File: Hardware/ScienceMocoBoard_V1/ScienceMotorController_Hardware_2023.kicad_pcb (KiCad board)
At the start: 2 copper layers, 124.6 x 81.3 mm, 134 parts, among them Q1 SI4156DY, Q10 SI4156DY, Q11 SI4156DY, Q12 SI4156DY, Q13 SI4156DY, Q14 SI4156DY, Q15 SI4156DY, Q16 SI4156DY, Q2 SI4156DY, Q3 SI4156DY, Q4 SI4156DY, Q5 SI4156DY, Q6 SI4156DY, Q7 SI4156DY, Q8 SI4156DY, Q9 SI4156DY, U1 IRS2005S, U10 IRS2005S, U11 TM4C129E_Launchpad, U2 IRS2005S, U3 3V3 OKI, U4 TSR_1-2450, U5 IRS2005S, U6 IRS2005S, U7 IRS2005S, U8 IRS2005S, U9 IRS2005S

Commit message: Started Layout Design
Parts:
- added G***: LOGO, MRDT_Silkscreens:0_MRDT_Logo_7.5mm, F.Cu at (-109.7, 145.0)
- added G***: LOGO, LOGO, F.Cu at (-106.2, 124.0)
- added G***: LOGO, LOGO, F.Cu at (-93.6, 73.5)
- moved D31 264.2 mm to (120.0, -125.0), turned to 180 degrees
- moved D30 244.6 mm to (120.0, -115.0), turned to 180 degrees
- moved LimSwitch6 243.3 mm to (105.0, -125.0)
- moved R38 233.6 mm to (115.0, -115.0)
- moved R39 231.2 mm to (115.0, -125.0)
- moved R37 203.8 mm to (115.0, -105.0)
- moved D29 201.0 mm to (120.0, -105.0), turned to 180 degrees
- moved LimSwitch5 187.1 mm to (105.0, -115.0)
- moved Re 186.1 mm to (115.0, -95.0)
- moved LimSwitch4 183.4 mm to (105.0, -105.0)
- moved LimSwitch2 181.3 mm to (105.0, -95.0)
- moved D27 179.3 mm to (120.0, -95.0), turned to 180 degrees
- moved R34 177.5 mm to (115.0, -85.0), turned to 180 degrees
- moved R36 171.0 mm to (115.0, -75.0)
- moved LimSwitch1 167.2 mm to (105.0, -85.0)
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- renumbered R35 to Re
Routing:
- removed copper zone on B.Cu, net GND
- removed copper zone on F.Cu, net GND
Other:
- board size 124.6 x 81.3 mm -> 187 x 127 mm

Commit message: Organized Layout
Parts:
- moved R16 280.5 mm to (54.6, 255.3), turned to 90 degrees
- moved D12 264.1 mm to (53.2, 283.1)
- moved C3 263.2 mm to (398.6, 120.8)
- moved C10 263.2 mm to (407.0, 116.9)
- moved Conn5 263.2 mm to (308.9, 134.3)
- moved Conn6 263.2 mm to (320.2, 116.7)
- moved D15 263.2 mm to (381.7, 136.3)
- moved D16 263.2 mm to (355.3, 139.3)
- moved D23 263.2 mm to (342.2, 139.4)
- moved D7 263.2 mm to (313.4, 126.5)
- moved Q12 263.2 mm to (375.2, 130.3)
- moved Q13 263.2 mm to (366.8, 131.8)
- moved Q14 263.2 mm to (366.8, 138.3)
- moved Q15 263.2 mm to (383.7, 122.8)
- moved R21 263.2 mm to (386.0, 136.2)
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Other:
- board text added: "Encoders"
- board text added: "Limit Swithches"
- board text added: "Power"
- board text added: "Servos"
- board text added: "X-Axis"

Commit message: Layout for Encoders, Servos, and Limit Switches
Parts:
- removed the G*** at (-109.7, 145.0)
- Conn1, Conn2, Conn3, Conn4, Conn5, Conn6, Conn7: footprint MRDT_Connectors:Square_Anderson_2_V_Side_By_Side -> MRDT_Connectors:Square_Anderson_2_H_Side_By_Side
- moved R39 260.8 mm to (91.8, 134.7), turned to 90 degrees
- moved D31 260.8 mm to (96.9, 134.7), turned to -90 degrees
- moved LimSwitch6 253.9 mm to (93.1, 128.7)
- moved R38 252.3 mm to (79.4, 134.7), turned to 90 degrees
- moved D30 252.1 mm to (85.5, 134.7), turned to -90 degrees
- moved D29 245.5 mm to (73.3, 136.0), turned to -90 degrees
- moved R37 245.1 mm to (68.3, 135.6), turned to 90 degrees
- moved LimSwitch5 245.1 mm to (81.3, 128.9)
- moved LimSwitch4 236.8 mm to (68.8, 129.0)
- moved D13 221.2 mm to (96.8, 87.0), turned to 90 degrees
- moved R19 217.8 mm to (101.9, 87.0), turned to -90 degrees
- moved D12 217.1 mm to (146.5, 87.0), turned to 90 degrees
- moved D27 215.2 mm to (96.6, 118.9), turned to -90 degrees
- moved R35 214.7 mm to (92.4, 118.5), turned to 90 degrees
- moved R18 214.6 mm to (151.5, 87.0), turned to -90 degrees
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- renumbered Re to R35
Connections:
- R36 pad 2: unconnected-(R36-Pad2) -> Limit_Switch_1
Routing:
- net GND: track 0.00 -> 86.5 mm
- net +5V: track 0.00 -> 74.6 mm
- net Servo_3: track 0.00 -> 46.0 mm, vias 0 -> 1
- net Servo_6: track 0.00 -> 37.5 mm
- net Limit_Switch_4: track 0.00 -> 37.2 mm
- net Limit_Switch_6: track 0.00 -> 35.1 mm
- net Limit_Switch_5: track 0.00 -> 33.2 mm
- net Servo_5: track 0.00 -> 27.1 mm
- net Limit_Switch_3: track 0.00 -> 27.0 mm
- net Encoder_PWM_4: track 0.00 -> 26.8 mm
- net Servo_2: track 0.00 -> 26.4 mm
- net Servo_1: track 0.00 -> 23.8 mm
- net +3V3: track 0.00 -> 23.1 mm
- net Limit_Switch_2: track 0.00 -> 19.2 mm
- net Limit_Switch_1: track 0.00 -> 18.0 mm
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- added copper zone on B.Cu, net GND
- added copper zone on F.Cu, net GND

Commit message: Power on Layout. Organized H-Bridge Components
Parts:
- moved U2 387.3 mm to (45.0, -37.1)
- moved C3 381.6 mm to (51.3, -37.3)
- moved Q3 366.3 mm to (65.3, -42.4)
- moved Q4 358.3 mm to (66.0, -32.0)
- moved D2 336.5 mm to (32.3, -40.1)
- moved D7 336.3 mm to (49.3, -42.7)
- moved D15 321.0 mm to (118.4, -47.2)
- moved D5 319.9 mm to (37.8, -40.1)
- moved R9 315.3 mm to (56.9, -34.3)
- moved R2 312.1 mm to (32.0, -34.5)
- moved R5 304.6 mm to (37.3, -33.8)
- moved R21 303.9 mm to (164.1, -71.4)
- moved U6 298.7 mm to (127.0, -36.3)
- moved R26 294.2 mm to (184.9, -79.2)
- moved C10 293.7 mm to (184.5, -74.8), turned to -90 degrees
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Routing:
- net GND: track 86.5 -> 29.6 mm
- net +3V3: track 23.1 -> 41.3 mm
- net +5V: track 74.6 -> 84.7 mm
- net +12V: track 0.00 -> 8.88 mm
- net Net-(D9-Pad2): track 0.00 -> 5.10 mm
- net Net-(D8-Pad2): track 0.00 -> 4.27 mm
- net Net-(D3-Pad2): track 0.00 -> 3.55 mm
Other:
- board size 187 x 127 mm -> 179.9 x 127 mm
- board text added: "Science-Z"
- board text added: "Scoop-Z"

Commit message: Attempted an H-Bridge
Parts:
- moved D1 134.5 mm to (65.8, 49.9), turned to 180 degrees
- moved D6 131.0 mm to (61.3, 44.6), turned to -90 degrees
- moved C5 129.7 mm to (99.1, 48.5), turned to 180 degrees
- moved R1 129.6 mm to (61.6, 49.9), turned to 180 degrees
- moved R4 127.4 mm to (82.7, 49.7)
- moved D4 127.4 mm to (77.2, 49.7)
- moved U1 127.1 mm to (71.2, 44.7), turned to 90 degrees
- moved R7 125.8 mm to (78.4, 42.2)
- moved Q1 122.0 mm to (85.6, 37.4), turned to 180 degrees
- moved Conn4 121.3 mm to (103.3, 43.9), turned to -90 degrees
- moved Q2 119.0 mm to (85.6, 43.5)
- moved C2 116.9 mm to (70.6, 38.4)
- moved R6 112.9 mm to (78.5, 38.2), turned to 0 degrees
- moved Q5 112.4 mm to (113.3, 31.0)
- moved D14 112.1 mm to (128.8, 27.9), turned to 180 degrees
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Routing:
- net +12V: track 8.88 -> 22.3 mm
- net Net-(C2-Pad1): track 0.00 -> 12.7 mm
- net RVS_PWM_1: track 0.00 -> 12.0 mm
- net FWD_PWM_1: track 0.00 -> 11.6 mm
- net Net-(R12-Pad1): track 0.00 -> 11.3 mm
- net /M-: track 0.00 -> 11.0 mm
- net /M+: track 0.00 -> 10.2 mm
- net Net-(R6-Pad1): track 0.00 -> 9.82 mm, vias 0 -> 2
- net Net-(Q1-Pad4): track 0.00 -> 9.76 mm
- net Net-(R13-Pad1): track 0.00 -> 9.49 mm
- net Net-(C7-Pad1): track 0.00 -> 8.66 mm
- net Net-(Q2-Pad4): track 0.00 -> 6.05 mm
- net Net-(Q5-Pad4): track 0.00 -> 4.61 mm
- net Net-(R7-Pad1): track 0.00 -> 4.38 mm
- net Net-(Q6-Pad4): track 0.00 -> 4.36 mm
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
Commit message: Reworked Layout to be better
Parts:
- moved D24 158.0 mm to (197.6, 122.2), turned to 90 degrees
- moved R32 157.9 mm to (197.6, 112.5), turned to -90 degrees
- moved D25 155.9 mm to (200.2, 127.5), turned to 90 degrees
- moved R33 155.2 mm to (200.2, 117.9), turned to 90 degrees
- moved R1 102.4 mm to (162.3, 68.6), turned to -90 degrees
- moved R37 99.0 mm to (153.2, 133.5)
- moved R38 98.0 mm to (163.3, 133.5)
- moved D6 96.6 mm to (156.5, 61.5)
- moved D1 96.4 mm to (160.4, 68.6), turned to 90 degrees
- moved LimSwitch4 95.9 mm to (150.6, 127.4)
- moved R39 95.8 mm to (173.5, 133.5)
- moved R7 94.8 mm to (173.2, 40.1), turned to 90 degrees
- moved LimSwitch5 93.7 mm to (160.8, 127.4)
- moved LimSwitch6 92.0 mm to (170.9, 127.4)
- moved D4 91.6 mm to (166.9, 68.6), turned to 90 degrees
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- renumbered D28 to D26, D26 to D27, D27 to D28, LimSwitch3 to LimSwitch1, LimSwitch1 to LimSwitch2, LimSwitch2 to LimSwitch3, R36 to R34, R34 to R35, R35 to R36
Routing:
- net +5V: track 84.7 -> 0.36 mm
- net Servo_3: track 46.0 -> 0.00 mm, vias 1 -> 0
- net +3V3: track 41.3 -> 0.00 mm
- net Servo_6: track 37.5 -> 0.00 mm
- net Limit_Switch_4: track 37.2 -> 0.00 mm
- net Limit_Switch_6: track 35.1 -> 0.00 mm
- net Limit_Switch_5: track 33.2 -> 0.00 mm
- net GND: track 29.6 -> 0.54 mm
- net Servo_5: track 27.1 -> 0.00 mm
- net Limit_Switch_3: track 27.0 -> 0.00 mm
- net Encoder_PWM_4: track 26.8 -> 0.00 mm
- net Servo_2: track 26.4 -> 0.00 mm
- net Servo_1: track 23.8 -> 0.00 mm
- net +12V: track 22.3 -> 0.00 mm
- net Limit_Switch_2: track 19.2 -> 0.00 mm
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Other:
- board size 179.9 x 127 mm -> 231.4 x 127 mm
- board text added: "Limit Switches"
- board text removed: "Limit Swithches"

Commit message: Added H-Bridges. Started Traces
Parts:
- Conn4, Conn5, Conn6, Conn7: moved to B.Cu
- moved D23 169.5 mm to (164.2, 60.4), turned to -90 degrees
- moved D5 162.2 mm to (159.0, 67.8)
- moved D2 160.9 mm to (151.6, 67.8)
- moved R5 159.6 mm to (159.0, 69.4), turned to 180 degrees
- moved R2 158.5 mm to (151.6, 69.4), turned to 180 degrees
- moved U10 158.2 mm to (167.9, 62.0), turned to 90 degrees
- moved R30 154.7 mm to (169.0, 55.6)
- moved C14 150.7 mm to (166.1, 56.4), turned to 90 degrees
- moved U2 149.9 mm to (157.5, 61.9), turned to 90 degrees
- moved Q15 148.8 mm to (167.9, 50.9), turned to 90 degrees
- moved D7 147.8 mm to (153.8, 61.7), turned to -90 degrees
- moved D19 145.3 mm to (177.5, 68.0)
- moved D17 145.1 mm to (169.5, 67.8)
- moved D21 141.9 mm to (172.2, 60.5), turned to -90 degrees
- moved R23 141.8 mm to (177.5, 69.8), turned to 180 degrees
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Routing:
- net Limit_Switch_6: track 0.00 -> 56.0 mm
- net Limit_Switch_5: track 0.00 -> 51.4 mm
- net Limit_Switch_4: track 0.00 -> 42.9 mm
- net Limit_Switch_3: track 0.00 -> 34.4 mm
- net Limit_Switch_2: track 0.00 -> 28.4 mm
- net Limit_Switch_1: track 0.00 -> 25.3 mm
- net Net-(D31-Pad2): track 0.00 -> 4.33 mm
- net Net-(D30-Pad2): track 0.00 -> 4.33 mm
- net Net-(D28-Pad2): track 0.00 -> 4.33 mm
- net Net-(D26-Pad2): track 0.00 -> 4.33 mm
- net Net-(D29-Pad2): track 0.00 -> 4.33 mm
- net Net-(D27-Pad2): track 0.00 -> 4.33 mm
- net Net-(D24-Pad2): track 0.00 -> 2.64 mm
- net Net-(D25-Pad2): track 0.00 -> 2.63 mm
- net Net-(R32-Pad1): track 0.00 -> 2.48 mm
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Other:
- board text added: "Spare"

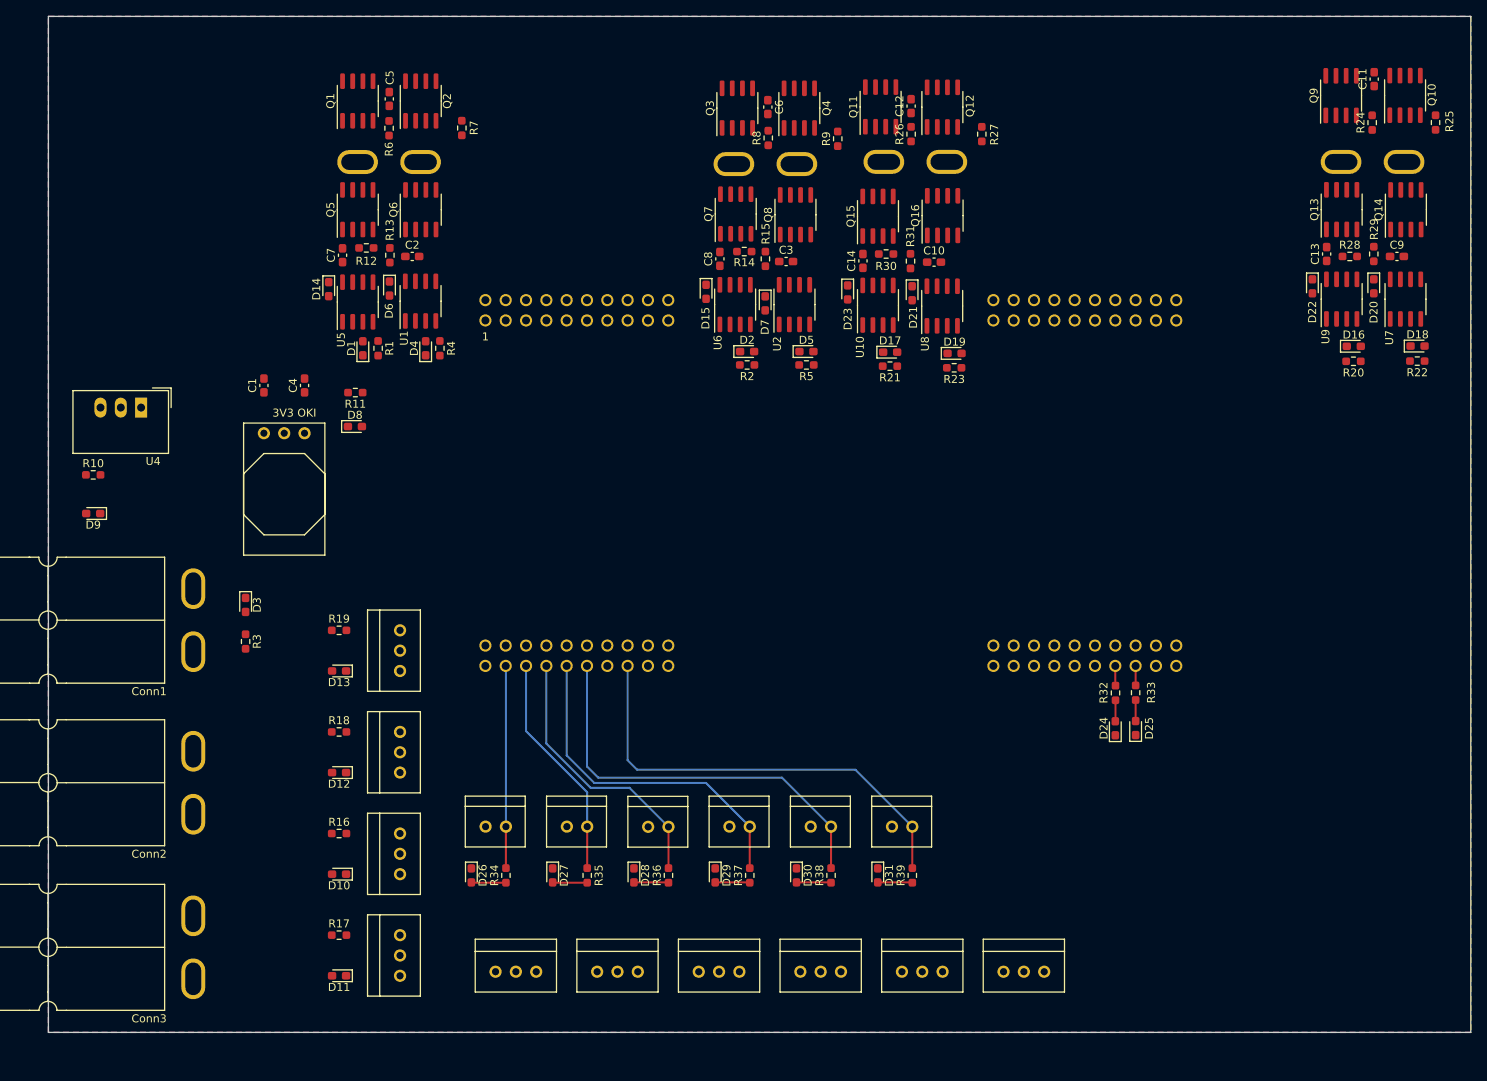
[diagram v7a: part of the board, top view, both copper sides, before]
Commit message: Made traces for servos and encoders
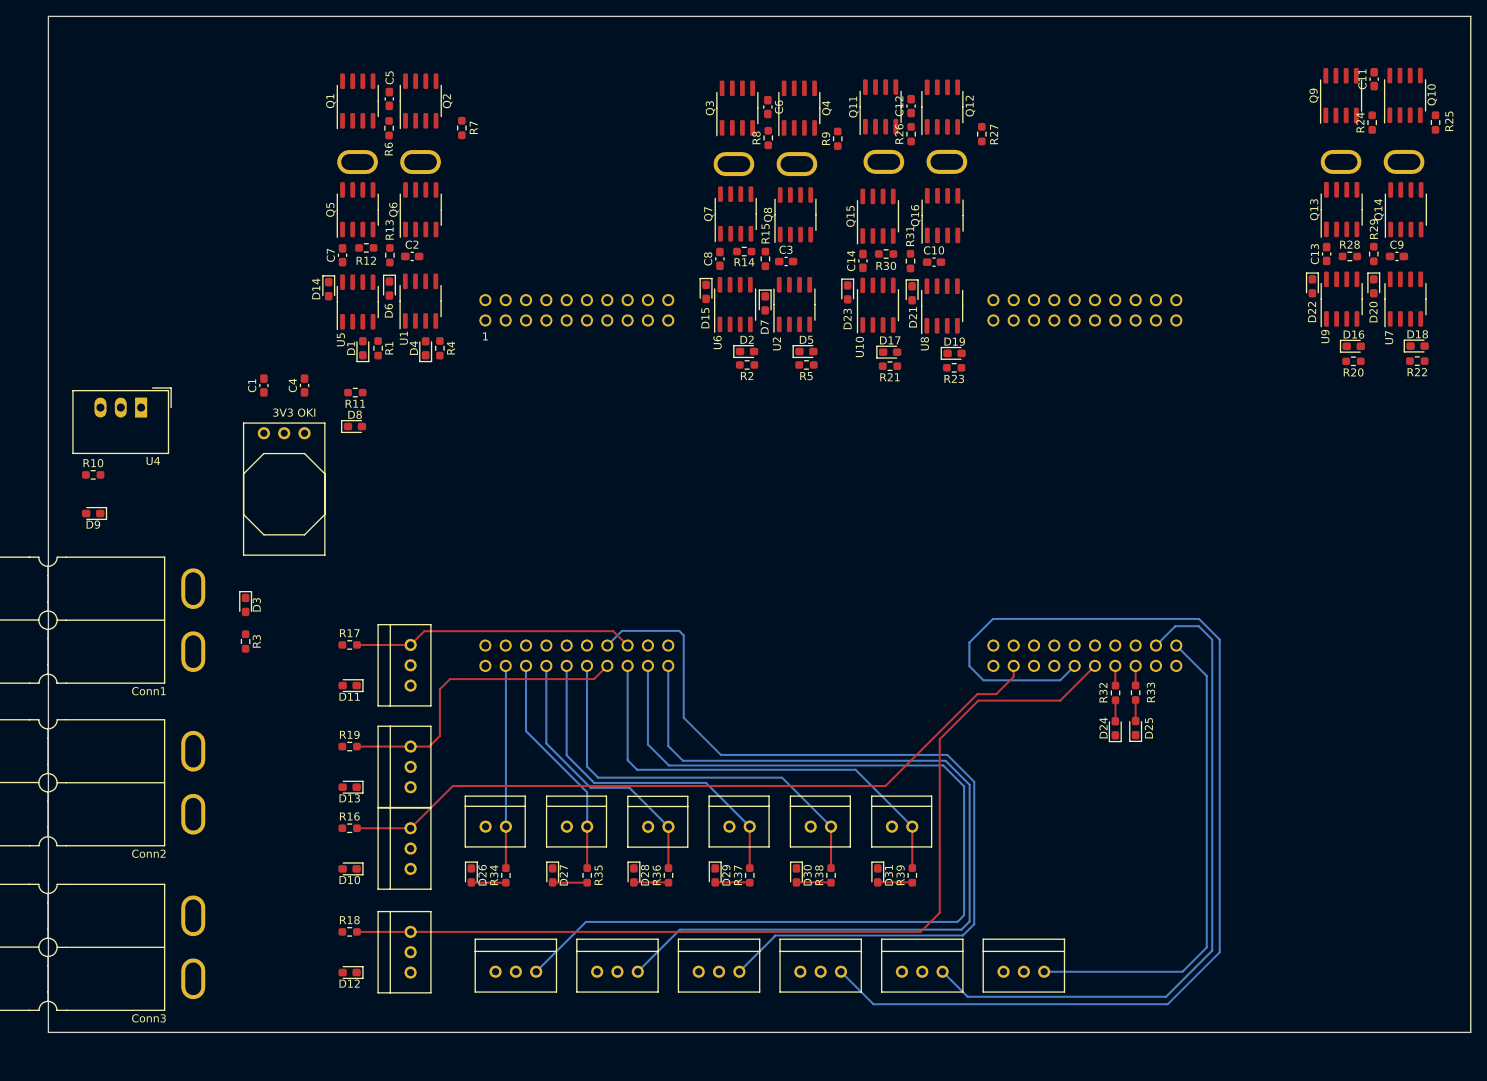
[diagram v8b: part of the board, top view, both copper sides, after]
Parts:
- moved R17 36.3 mm to (101.9, 104.4)
- moved AbsEncode1 36.3 mm to (109.5, 109.5)
- moved D11 36.3 mm to (101.9, 109.5)
- moved AbsEncode2 25.0 mm to (109.5, 145.4)
- moved D12 25.0 mm to (101.9, 145.4)
- moved R18 25.0 mm to (101.9, 140.3)
- moved AbsEncode3 14.6 mm to (109.5, 122.2)
- moved D13 14.6 mm to (101.9, 122.2)
- moved R19 14.6 mm to (101.9, 117.1)
- moved AbsEncode4 1.48 mm to (109.5, 132.4)
- moved D10 1.48 mm to (101.9, 132.4)
- moved R16 1.48 mm to (101.9, 127.4)
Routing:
- net Servo_4: track 0.00 -> 142.0 mm
- net Servo_1: track 0.00 -> 124.0 mm
- net Encoder_PWM_3: track 0.00 -> 118.7 mm
- net Servo_2: track 0.00 -> 110.9 mm
- net Servo_3: track 0.00 -> 110.1 mm
- net Encoder_PWM_2: track 0.00 -> 91.3 mm
- net Servo_5: track 0.00 -> 85.0 mm
- net Servo_6: track 0.00 -> 60.9 mm
- net Encoder_PWM_4: track 0.00 -> 38.9 mm
- net Encoder_PWM_1: track 0.00 -> 35.3 mm
- removed copper zone on B.Cu, net GND
- removed copper zone on F.Cu, net GND
